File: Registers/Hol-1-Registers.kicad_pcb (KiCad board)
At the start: 2 copper layers, 109.2 x 78.7 mm, 26 parts, among them P1 DATA BUS, P2 REG-A-CTRL, P3 REG-B-CTRL, P4 REG-C-CTRL, P5 POWER, P6 CTRL-ALL, P7 REGISTER A LINK, P8 REGISTER B LINK, U1 74LS245, U2 74LS245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

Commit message: v1.3.5 Registers PCB image
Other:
- board text added: "CLK/CLR"
- board text added: "I/O Reg A"
- board text added: "I/O Reg B"
- board text added: "I/O Reg C"
- board text removed: "CLK & CLR"
- board text removed: "Reg A I/O"
- board text removed: "Reg B I/O"
- board text removed: "Reg C I/O"
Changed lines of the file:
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@@
     (links 195)
     (no_connects 0)
-    (area 84.127143 63.449999 209.292857 142.290001)
+    (area 84.127143 63.449999 216.149999 142.290001)
     (thickness 1.6)
     (drawings 15)
@@
     )
   )
-  (gr_text "CLK & CLR" (at 187.96 135.89) (layer F.SilkS)
+  (gr_text "  Hol-1 8-bit CPU     Registers\nwww.benningtons.net  Rev 1.0" (at 168.91 66.04) (layer F.SilkS)
     (effects (font (size 1.5 1.5) (thickness 0.3)))
   )
-  (gr_text "Reg C\n I/O" (at 184.15 116.84) (layer F.SilkS)
+  (gr_text CLK/CLR (at 189.23 135.89) (layer F.SilkS)
     (effects (font (size 1.5 1.5) (thickness 0.3)))
   )
-  (gr_text "Reg B\n I/O" (at 184.15 91.44) (layer F.SilkS)
+  (gr_text " I/O\nReg C\n" (at 189.23 123.19 90) (layer F.SilkS)
     (effects (font (size 1.5 1.5) (thickness 0.3)))
   )
-  (gr_text "Reg A\n I/O" (at 184.15 66.04) (layer F.SilkS)
+  (gr_text " I/O\nReg B\n" (at 189.23 97.79 90) (layer F.SilkS)
+    (effects (font (size 1.5 1.5) (thickness 0.3)))
+  )
+  (gr_text " I/O\nReg A\n" (at 189.23 72.39 90) (layer F.SilkS)
     (effects (font (size 1.5 1.5) (thickness 0.3)))
   )
@@
     (effects (font (size 1.5 1.5) (thickness 0.3)))
   )
-  (gr_text "Hol-1 8-bit CPU                  Registers\nwww.benningtons.net               Rev 1.0" (at 190.5 104.14 90) (layer F.SilkS)
-    (effects (font (size 1.5 1.5) (thickness 0.3)))
-  )

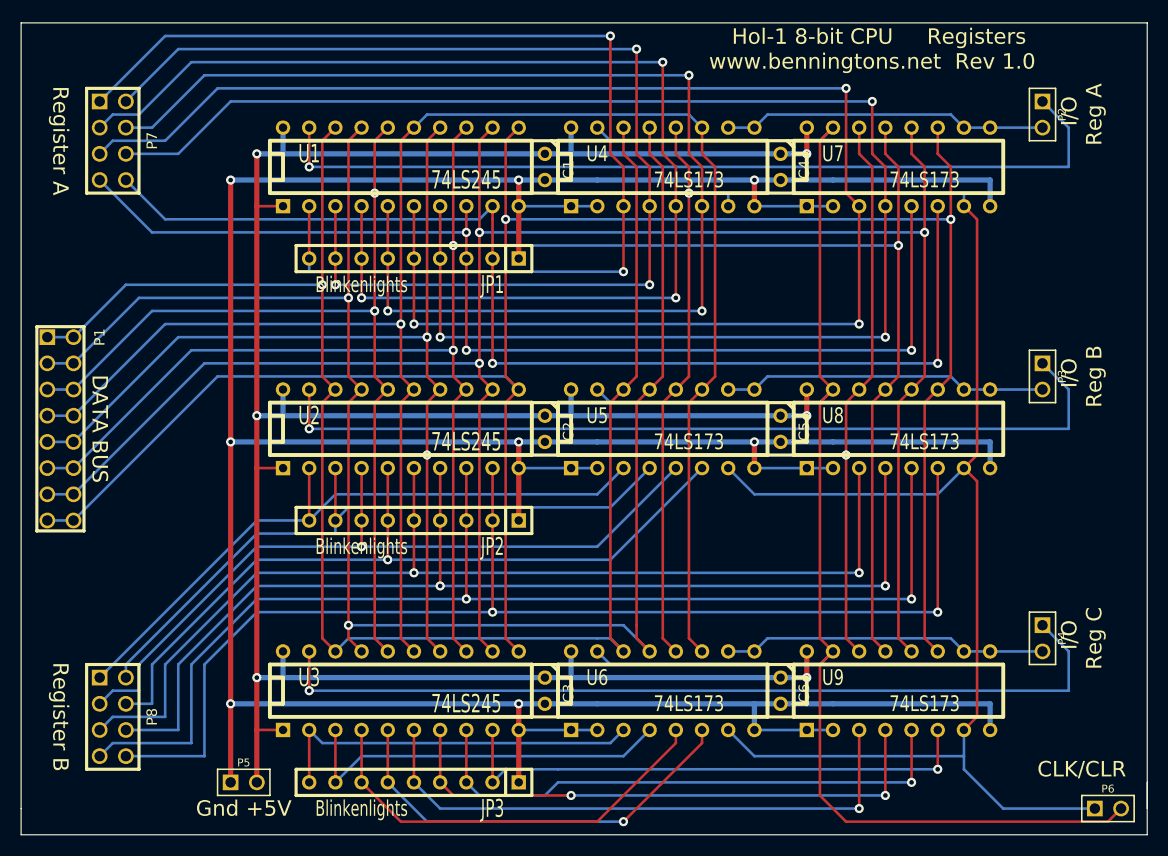
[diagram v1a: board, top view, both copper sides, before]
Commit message: v1.5.14 Registers: Re-numbered A & B ports. ALU to follow
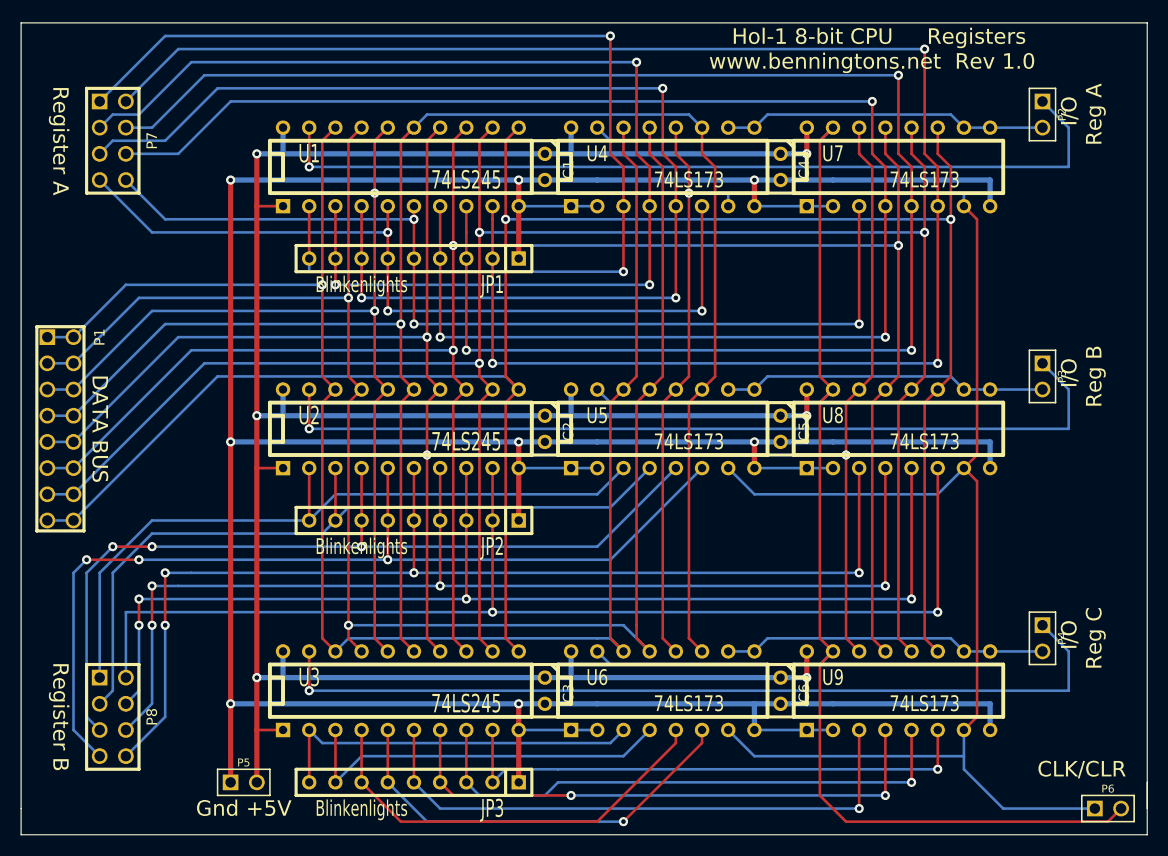
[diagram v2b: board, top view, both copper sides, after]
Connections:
- P7 pad 2: /A2 -> /A8
- P7 pad 3: /A3 -> /A2
- P7 pad 4: /A4 -> /A7
- P7 pad 5: /A5 -> /A3
- P7 pad 7: /A7 -> /A4
- P7 pad 8: /A8 -> /A5
- P8 pad 2: /B2 -> /B8
- P8 pad 3: /B3 -> /B2
- P8 pad 4: /B4 -> /B7
- P8 pad 5: /B5 -> /B3
- P8 pad 7: /B7 -> /B4
- P8 pad 8: /B8 -> /B5
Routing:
- net /A8: track 111.3 -> 169.0 mm, vias 2 -> 3
- net /A5: track 153.0 -> 95.6 mm
- net /A7: track 108.8 -> 161.4 mm
- net /A4: track 120.7 -> 80.8 mm
- net /B4: track 76.5 -> 92.9 mm, vias 1 -> 3
- net /B3: track 74.5 -> 84.7 mm, vias 1 -> 3
- net /B2: track 65.8 -> 74.6 mm
- net /B1: track 64.3 -> 70.2 mm
- net /B8: track 117.7 -> 113.0 mm
- net /B7: track 114.9 -> 111.0 mm, vias 2 -> 4
- net /B5: track 103.3 -> 107.0 mm, vias 2 -> 4
- net /B6: track 106.0 -> 109.0 mm, vias 2 -> 4
- net /A3: track 120.0 -> 117.5 mm
- net /A2: track 113.1 -> 114.9 mm

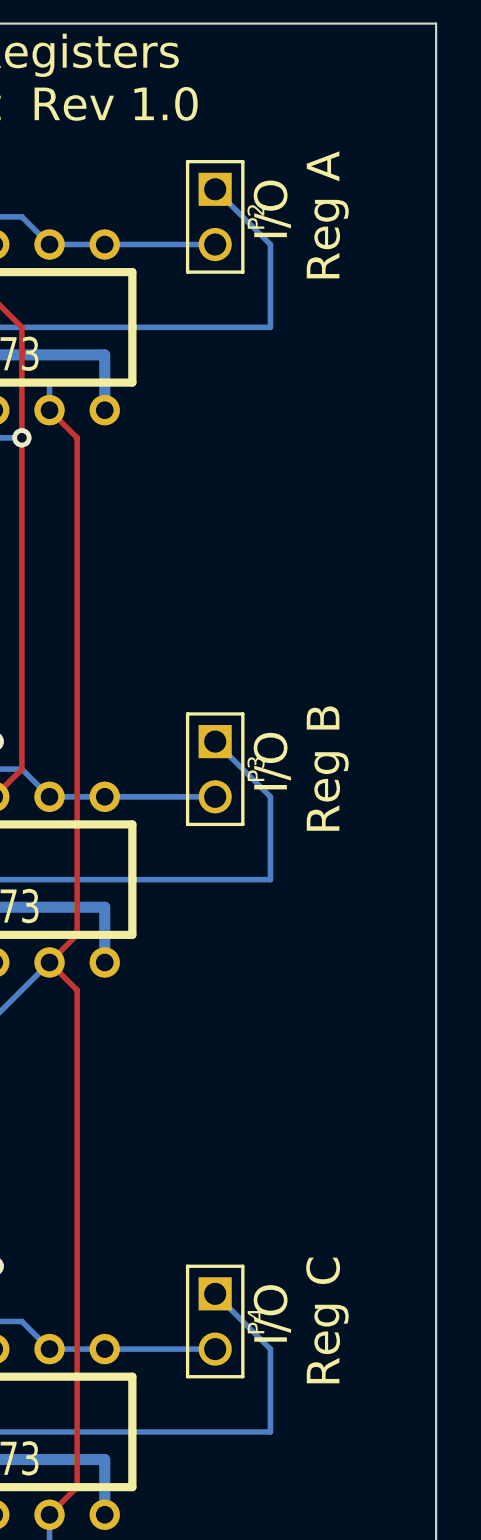
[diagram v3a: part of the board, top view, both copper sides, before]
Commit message: v1.5.19 upgraded to KiCad 5.0
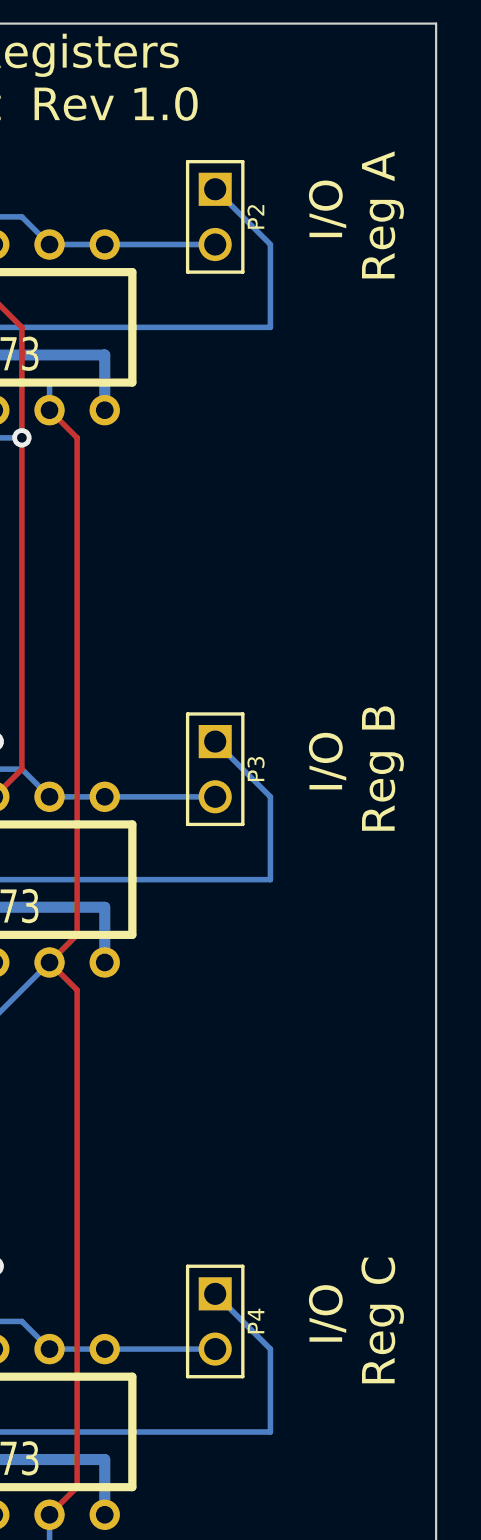
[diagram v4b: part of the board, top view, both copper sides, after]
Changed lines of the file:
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@@
-(kicad_pcb (version 4) (host pcbnew 4.0.5+dfsg1-4)
+(kicad_pcb (version 20171130) (host pcbnew 5.0.2+dfsg1-1+deb10u1)
   (general
-    (links 195)
-    (no_connects 0)
-    (area 86.309999 63.449999 195.630001 142.290001)
     (thickness 1.6)
     (drawings 15)
@@
     (pad_drill 1.016)
     (pad_to_mask_clearance 0)
+    (solder_mask_min_width 0.25)
     (aux_axis_origin 86.36 63.5)
     (visible_elements FFFFFF3F)
@@
       (layerselection 0x00030_80000001)
       (usegerberextensions true)
+      (usegerberattributes false)
+      (usegerberadvancedattributes false)
+      (creategerberjobfile false)
       (excludeedgelayer true)
       (linewidth 0.150000)
@@
       (hpglpennumber 1)
       (hpglpenspeed 20)
-      (hpglpendiameter 15)
-      (hpglpenoverlay 2)
+      (hpglpendiameter 15.000000)
       (psnegative false)
       (psa4output false)
@@
     (effects (font (size 1.5 1.5) (thickness 0.3)))
   )
-  (gr_text " I/O\nReg C\n" (at 189.23 123.19 90) (layer F.SilkS)
+  (gr_text " I/O\nReg C\n" (at 191.77 123.19 90) (layer F.SilkS)
     (effects (font (size 1.5 1.5) (thickness 0.3)))
   )
-  (gr_text " I/O\nReg B\n" (at 189.23 97.79 90) (layer F.SilkS)
+  (gr_text " I/O\nReg B\n" (at 191.77 97.79 90) (layer F.SilkS)
     (effects (font (size 1.5 1.5) (thickness 0.3)))
   )
-  (gr_text " I/O\nReg A\n" (at 189.23 72.39 90) (layer F.SilkS)
+  (gr_text " I/O\nReg A\n" (at 191.77 72.39 90) (layer F.SilkS)
     (effects (font (size 1.5 1.5) (thickness 0.3)))
   )

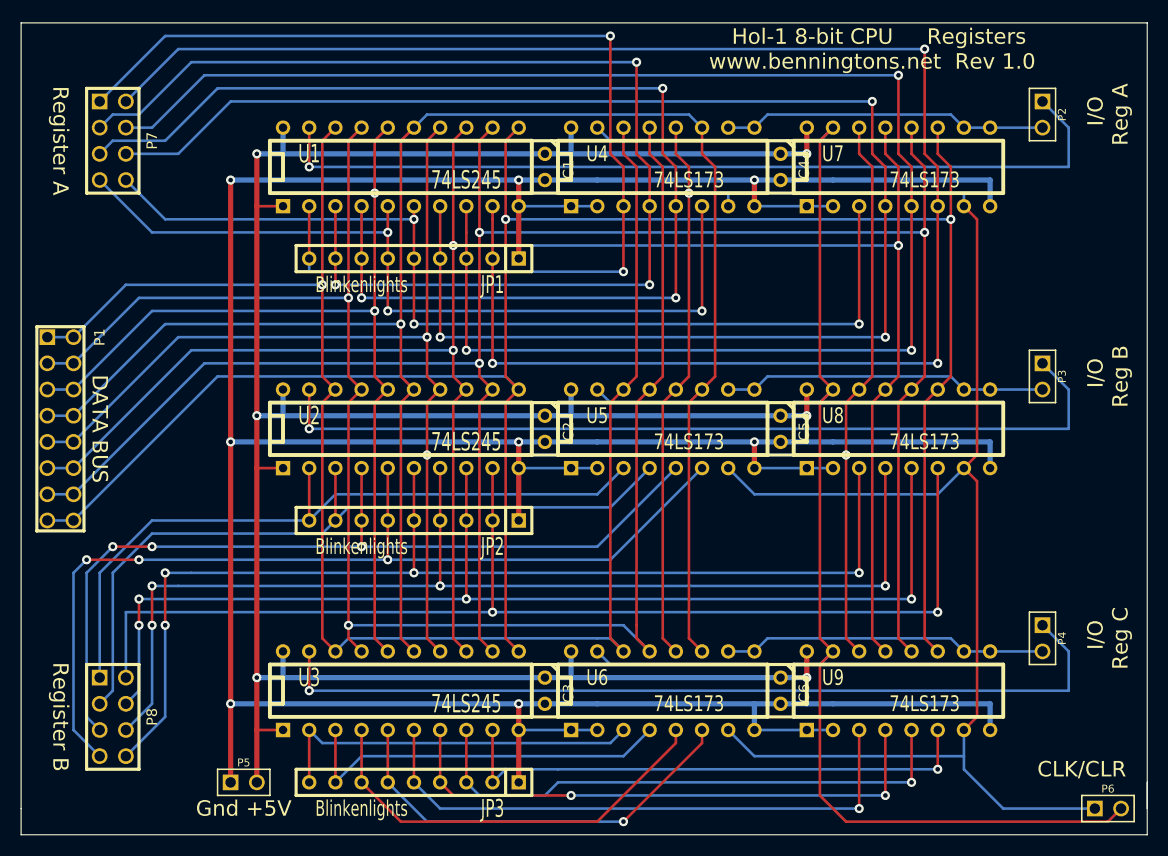
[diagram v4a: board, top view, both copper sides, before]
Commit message: 1.5.21 upgraded to KiCad 6.0
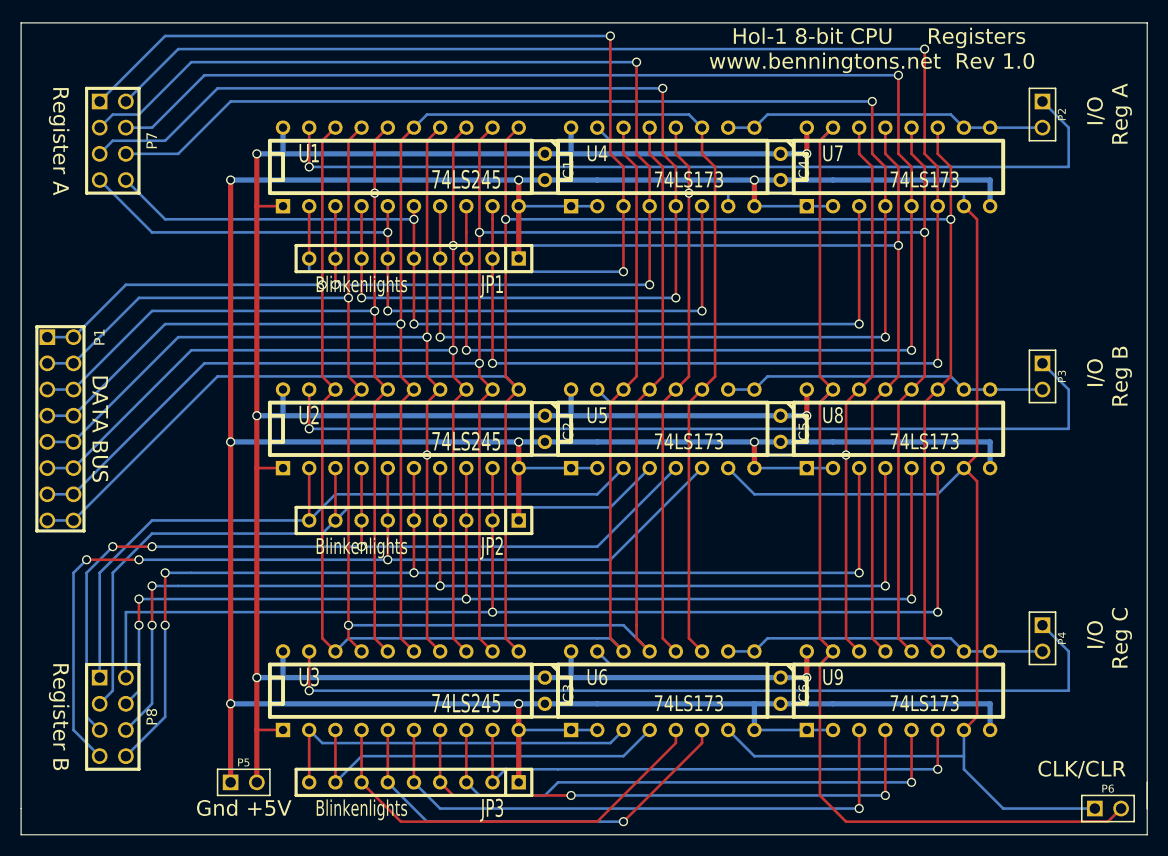
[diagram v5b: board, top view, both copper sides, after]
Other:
- net class Default removed
